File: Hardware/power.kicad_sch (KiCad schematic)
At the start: 56 parts, among them U1 H616, U3 AXP305

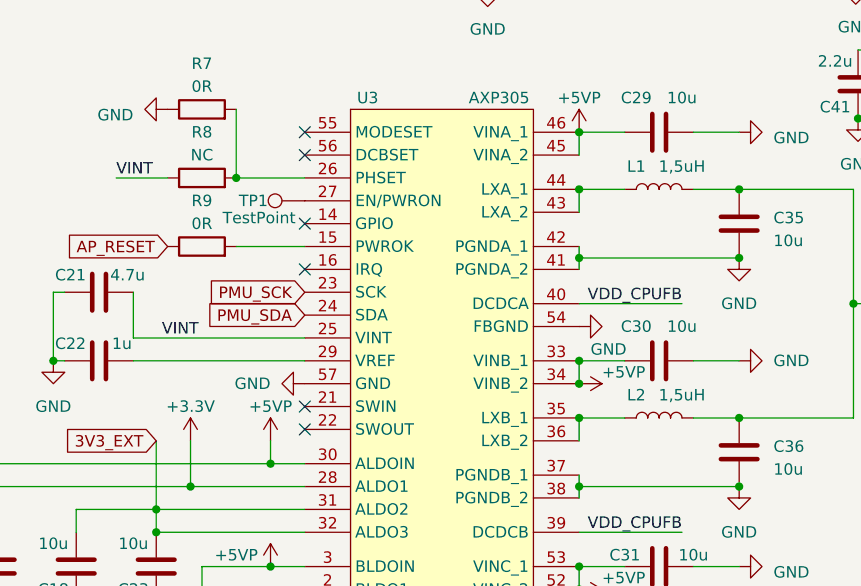
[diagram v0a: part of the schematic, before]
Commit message: fixed crystal resonator value
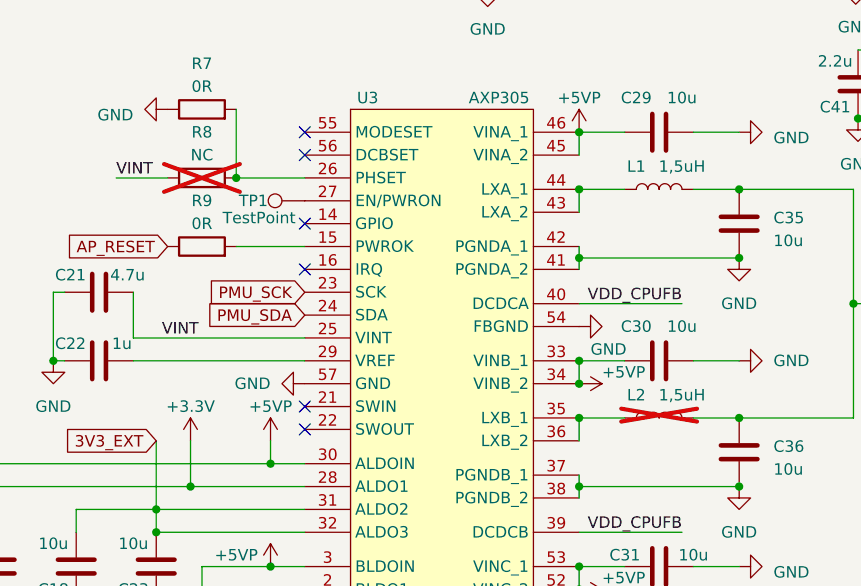
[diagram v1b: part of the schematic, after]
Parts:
- L2, R8: now not fitted
